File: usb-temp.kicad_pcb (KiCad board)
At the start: 4 copper layers, 40 x 12.7 mm, 25 parts, among them J1 Conn_01x02_Pin, J10 Conn_01x02_Pin, J2 USB_MB, J3 Conn_01x05, J4 Conn_01x02_Pin, J5 Conn_01x02_Pin, J6 Conn_01x02_Pin, J7 Conn_01x02_Pin, J8 Conn_01x02_Pin, J9 Conn_01x02_Pin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

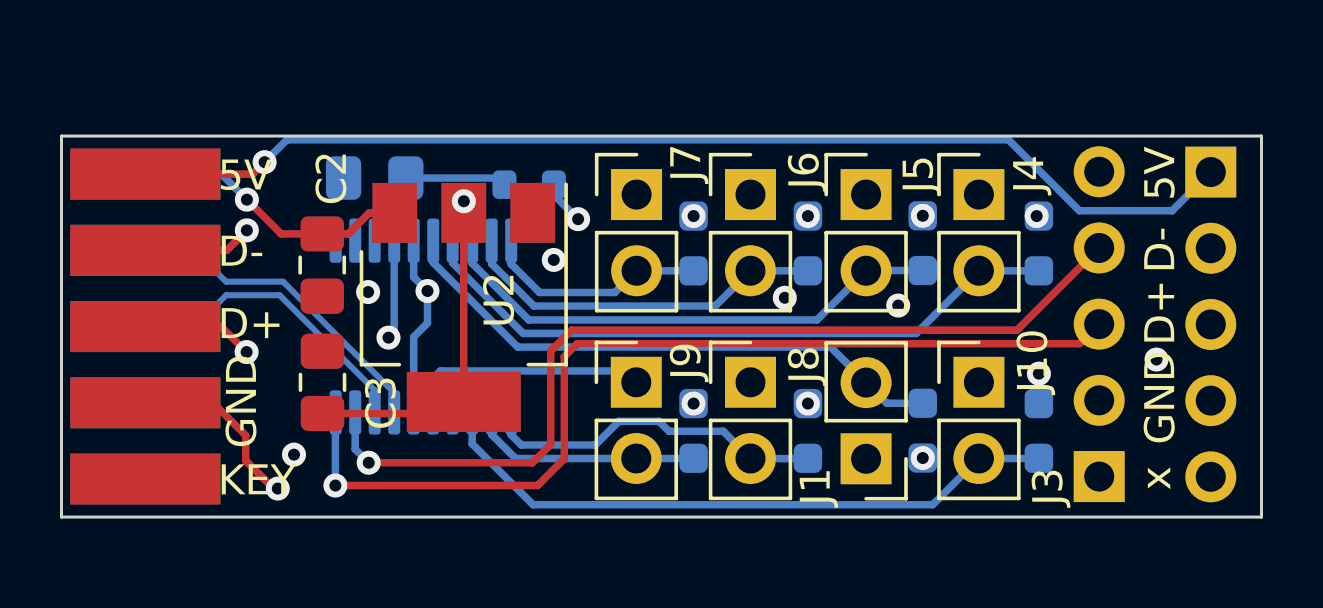
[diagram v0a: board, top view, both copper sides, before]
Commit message: Switching to new desing, small swd
working on v2.0
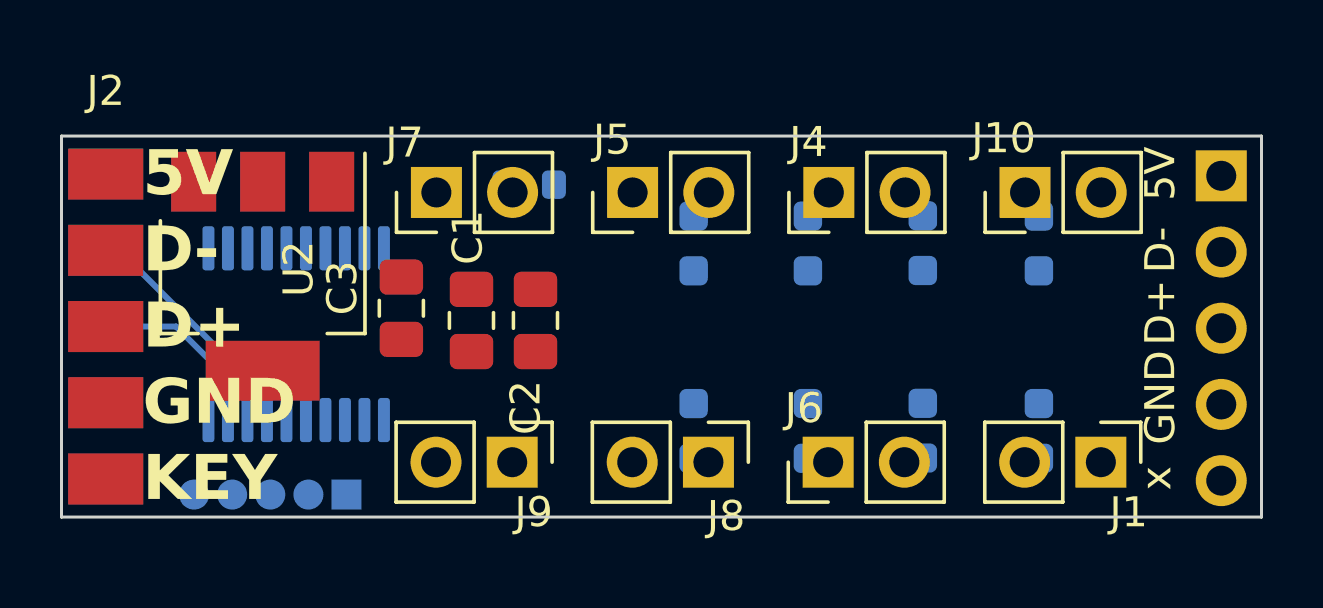
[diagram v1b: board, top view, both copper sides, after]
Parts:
- removed J3: Conn_01x05, Connector_PinHeader_2.54mm:PinHeader_1x05_P2.54mm_Vertical
- added U3: ~, eurorack:1.27 SWD Programmer, B.Cu at (9.50, 12.0)
- C1: moved to F.Cu
- J2: footprint MyLibs:MB_USB -> eurorack:MB_USB
- U1: value STM32F042F4Px -> STM32F042F6Px
- U2: value ZLDO1117G33TA -> MCP1799T-3302H/DB
- moved J6 9.29 mm to (25.6, 10.9), turned to 90 degrees
- moved J1 7.83 mm to (34.6, 10.9), turned to -90 degrees
- moved J5 7.78 mm to (19.0, 1.88), turned to 90 degrees
- moved C2 7.34 mm to (15.8, 6.15), turned to 90 degrees
- moved U2 6.78 mm to (6.71, 4.67)
- moved J7 6.67 mm to (12.5, 1.88), turned to 90 degrees
- moved J10 6.51 mm to (32.1, 1.88), turned to 90 degrees
- moved C1 5.74 mm to (13.7, 6.15), turned to -90 degrees
- moved J4 5.00 mm to (25.6, 1.88), turned to 90 degrees
- moved J9 4.92 mm to (15.0, 10.9), turned to -90 degrees
- moved U1 4.25 mm to (7.82, 6.60)
- moved C3 3.61 mm to (11.3, 5.74), turned to -90 degrees
- moved J8 3.01 mm to (21.6, 10.9), turned to -90 degrees
- moved J2 1.32 mm to (1.47, 1.27)
- moved USB_2_Out1 0.37 mm to (38.7, 1.33)
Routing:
- net +3V3: track 81.6 -> 0.00 mm, vias 11 -> 0
- net Net-(J2A-D+): track 43.8 -> 0.00 mm, vias 1 -> 0
- net Net-(J2A-GND): track 39.7 -> 0.00 mm, vias 1 -> 0
- net Net-(J2A-D-): track 38.5 -> 0.00 mm, vias 1 -> 0
- net RST: track 38.0 -> 0.00 mm, vias 1 -> 0
- net Net-(J2A-VBUS): track 37.5 -> 0.00 mm, vias 1 -> 0
- net SWDCLK: track 32.1 -> 0.00 mm, vias 1 -> 0
- net SWDIO: track 31.0 -> 0.00 mm, vias 1 -> 0
- net /A_Input1/A: track 22.1 -> 0.00 mm
- net /A_Input7/A: track 21.4 -> 0.00 mm
- net /A_Input0/A: track 19.0 -> 0.00 mm
- net /A_Input2/A: track 17.2 -> 0.00 mm
- net /A_Input3/A: track 12.4 -> 0.00 mm
- net /A_Input5/A: track 11.6 -> 0.00 mm
- net +5V: track 9.43 -> 0.00 mm, vias 1 -> 0
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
